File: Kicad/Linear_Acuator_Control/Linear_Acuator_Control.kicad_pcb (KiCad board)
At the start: 2 copper layers, 89.5 x 68 mm, 10 parts, among them K1 RT42xAxx, K3 RT42xAxx, Q1 IRLZ44N, Q2 IRLZ44N, U1 ESP32-S3-WROOM

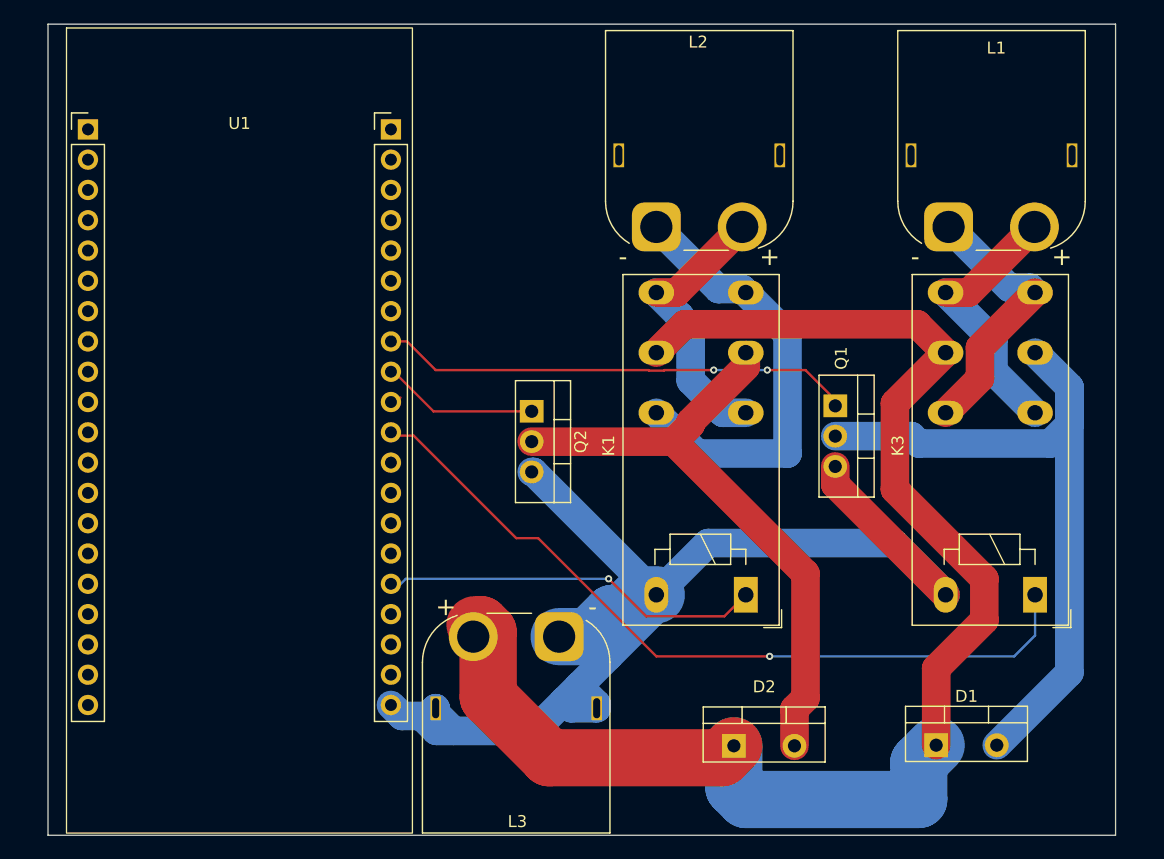
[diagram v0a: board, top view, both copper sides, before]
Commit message: Rerouting dodgy traces, fixing ESP32 footprint
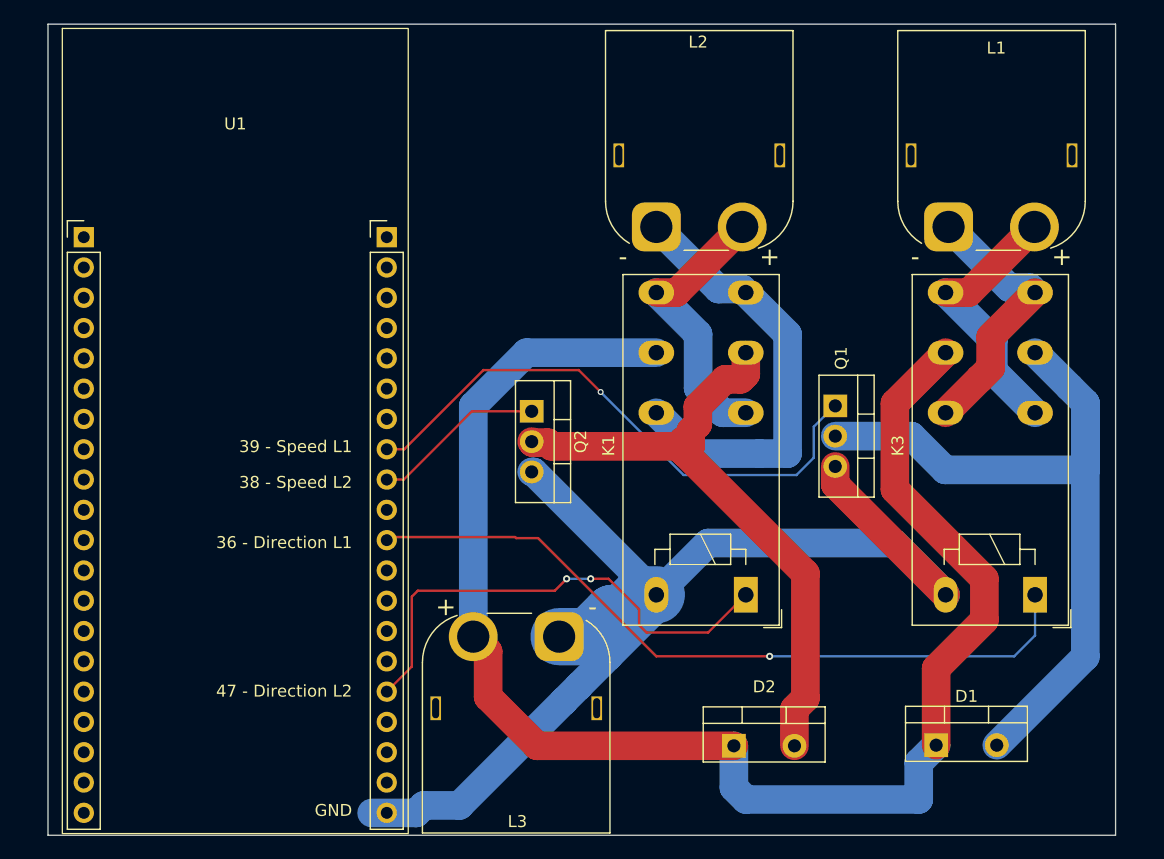
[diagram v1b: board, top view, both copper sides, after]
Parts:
- moved U1 0.56 mm to (79.2, 45.4)
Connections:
- net +3V3 renamed Net-(U1-3V3-Pad1)
- L3 pad : GND -> (no net)
- U1 pad 44: GND -> (no net)
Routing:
- net Dir L2: track 31.3 -> 41.4 mm, vias 1 -> 2
- net +24V: track 120.2 -> 129.3 mm
- net Speed L1: track 39.1 -> 48.0 mm, vias 2 -> 1
- net GND: track 107.5 -> 101.6 mm
- net Net-(D1-A): track 60.3 -> 65.6 mm
- net Dir L1: track 66.4 -> 62.7 mm
- net Net-(D2-A): track 52.1 -> 54.4 mm
- net Speed L2: track 13.4 -> 14.5 mm
- net unconnected-(U1-GPIO40/MTDO-Pad37): track 0.56 -> 0.00 mm
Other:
- board text added: "36 - Direction L1"
- board text added: "38 - Speed L2"
- board text added: "39 - Speed L1"
- board text added: "47 - Direction L2"
- board text added: "GND"

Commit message: Changed Mosfets to better suit 3.3v logic levels
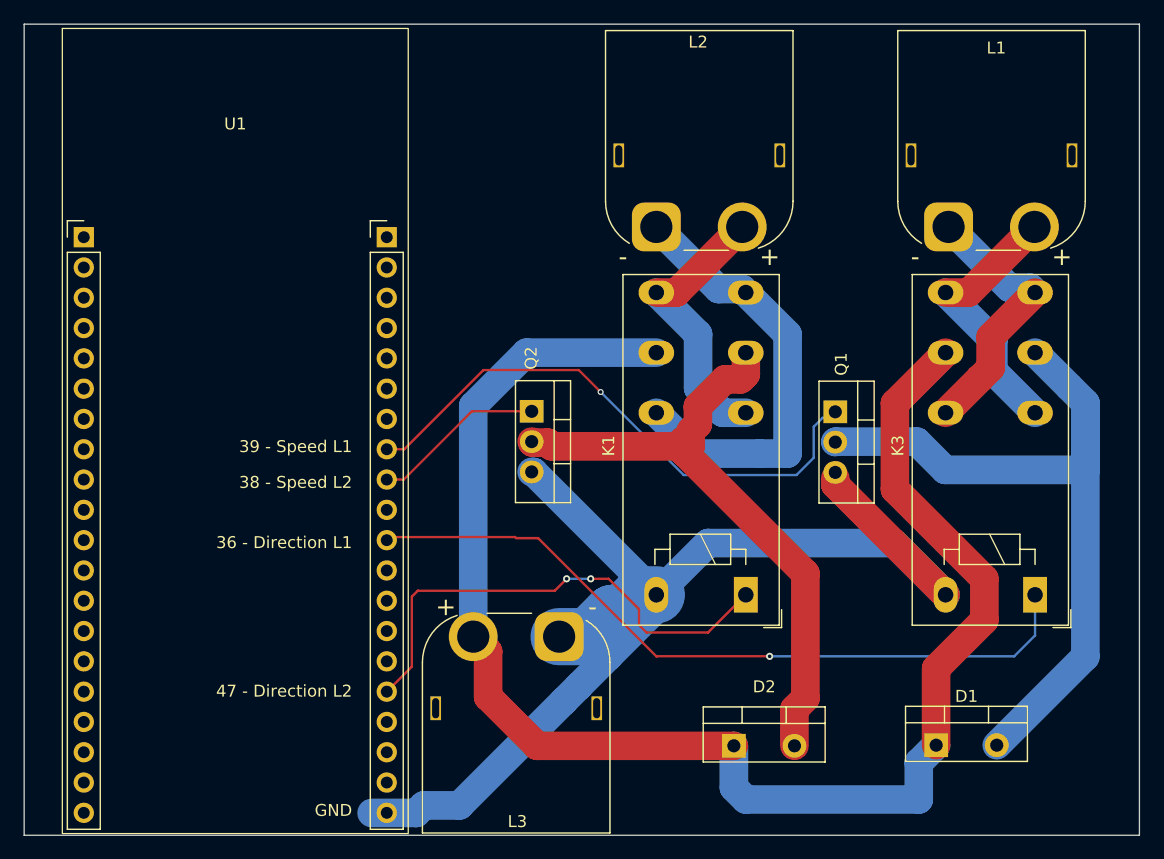
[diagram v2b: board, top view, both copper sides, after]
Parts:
- Q1, Q2: value IRLZ44N -> IRLB3813
- moved Q1 0.50 mm to (129.5, 69.5)
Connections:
- U1 pad 36: Dir L1 -> unconnected-(U1-GPIO39/MTCK-Pad36)
- U1 pad 39: Speed L1 -> unconnected-(U1-GPIO42/MTMS-Pad39)
- U1 pad 47: Dir L2 -> (no net)
- U1 pad GND: GND -> unconnected-(U1-PadGND)
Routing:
- net GND: track 101.6 -> 100.6 mm
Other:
- board size 89.5 x 68 mm -> 93.5 x 68 mm
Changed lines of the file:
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@@
 	(net 37 "unconnected-(U1-GPIO12{slash}ADC2_CH1-Pad18)")
 	(net 38 "Net-(U1-3V3-Pad1)")
+	(net 39 "unconnected-(U1-GPIO42{slash}MTMS-Pad39)")
+	(net 40 "unconnected-(U1-PadGND)")
+	(net 41 "unconnected-(U1-GPIO39{slash}MTCK-Pad36)")
 	(footprint "Relay_THT:Relay_DPDT_Schrack-RT2-FormC_RM5mm"
 		(layer "F.Cu")
@@
 		)
 		(property "Value" "RT42xAxx"
-			(at 12.192 4.25 90)
+			(at 0.84 4.5 90)
 			(layer "F.Fab")
 			(effects
@@
 	(footprint "Package_TO_SOT_THT:TO-220-3_Vertical"
 		(layer "F.Cu")
-		(at 129.5 69 -90)
+		(at 129.5 69.5 -90)
 		(descr "TO-220-3, Vertical, RM 2.54mm, see https://www.vishay.com/docs/66542/to-220-1.pdf, generated with kicad-footprint-generator TO_SOT_THT_generate.py")
 		(tags "TO-220-3 Vertical RM 2.54mm")
@@
 			)
 		)
-		(property "Value" "IRLZ44N"
+		(property "Value" "IRLB3813"
 			(at 2.54 2.2 90)
 			(layer "F.Fab")
@@
 		(tags "TO-220-3 Vertical RM 2.54mm")
 		(property "Reference" "Q2"
-			(at 2.54 -4.1 90)
+			(at -4.46 0.05 90)
 			(layer "F.SilkS")
 			(effects
@@
 			)
 		)
-		(property "Value" "IRLZ44N"
+		(property "Value" "IRLB3813"
 			(at 2.54 2.2 90)
 			(layer "F.Fab")
@@
 		)
 		(fp_text user "${REFERENCE}"
-			(at 0 2.98 0)
-			(unlocked yes)
+			(at 12.7 33.61 90)
 			(layer "F.Fab")
 			(effects
@@
 		)
 		(fp_text user "${REFERENCE}"
-			(at 12.7 33.61 90)
+			(at 0 2.98 0)
+			(unlocked yes)
 			(layer "F.Fab")
 			(effects
@@
 			(layers "*.Cu" "*.Mask")
 			(remove_unused_layers no)
-			(net 7 "Dir L1")
+			(net 41 "unconnected-(U1-GPIO39{slash}MTCK-Pad36)")
 			(pinfunction "GPIO39/MTCK")
 			(pintype "bidirectional")
@@
 			(layers "*.Cu" "*.Mask")
 			(remove_unused_layers no)
-			(net 11 "Speed L1")
+			(net 39 "unconnected-(U1-GPIO42{slash}MTMS-Pad39)")
 			(pinfunction "GPIO42/MTMS")
 			(pintype "bidirectional")
@@
 			(layers "*.Cu" "*.Mask")
 			(remove_unused_layers no)
-			(net 9 "Dir L2")
 		)
 		(pad "48" thru_hole circle
@@
 			(layers "*.Cu" "*.Mask")
 			(remove_unused_layers no)
-			(net 6 "GND")
+			(net 40 "unconnected-(U1-PadGND)")
 			(pinfunction "GND")
 			(pintype "power_in")
@@
 	)
 	(gr_line
-		(start 63.5 105)
-		(end 63.5 37)
+		(start 61.5 105)
+		(end 61.5 37)
 		(stroke
 			(width 0.05)
@@
 	)
 	(gr_line
-		(start 153 105)
-		(end 63.5 105)
+		(start 155 105)
+		(end 61.5 105)
 		(stroke
 			(width 0.05)
@@
 	)
 	(gr_line
-		(start 63.5 37)
-		(end 153 37)
+		(start 61.5 37)
+		(end 155 37)
 		(stroke
 			(width 0.05)
@@
 	)
 	(gr_line
-		(start 153 37)
-		(end 153 105)
+		(start 155 37)
+		(end 155 105)
 		(stroke
 			(width 0.05)
@@
 	)
 	(segment
-		(start 137.96 91.007266)
-		(end 137.96 97.45)
-		(width 2.4)
-		(layer "F.Cu")
-		(net 1)
-	)
-	(segment
 		(start 100.4 89.6)
 		(end 99.15 88.35)
@@
 	)
 	(segment
-		(start 142 86.967266)
-		(end 137.96 91.007266)
+		(start 142 83.5)
+		(end 142 86.967266)
 		(width 2.4)
 		(layer "F.Cu")
@@
 	)
 	(segment
-		(start 134.5 76)
-		(end 142 83.5)
+		(start 134.5 68.79)
+		(end 134.5 76)
 		(width 2.4)
 		(layer "F.Cu")
@@
 	)
 	(segment
-		(start 142 83.5)
-		(end 142 86.967266)
+		(start 142 86.967266)
+		(end 137.96 91.007266)
+		(width 2.4)
+		(layer "F.Cu")
+		(net 1)
+	)
+	(segment
+		(start 134.5 76)
+		(end 142 83.5)
 		(width 2.4)
 		(layer "F.Cu")
@@
 	)
 	(segment
-		(start 134.5 68.79)
-		(end 134.5 76)
+		(start 137.96 91.007266)
+		(end 137.96 97.45)
 		(width 2.4)
 		(layer "F.Cu")
@@
 	)
 	(segment
-		(start 135.885 71.54)
-		(end 138.714117 74.369117)
+		(start 138.714117 74.369117)
+		(end 150.407917 74.369117)
 		(width 2.4)
 		(layer "B.Cu")
@@
 	)
 	(segment
-		(start 150.407917 74.369117)
-		(end 150.465945 74.427145)
+		(start 150.465945 90.024055)
+		(end 150.465945 68.755945)
 		(width 2.4)
 		(layer "B.Cu")
@@
 	)
 	(segment
-		(start 129.5 71.54)
-		(end 135.885 71.54)
+		(start 136.345 72)
+		(end 138.714117 74.369117)
 		(width 2.4)
 		(layer "B.Cu")
@@
 	)
 	(segment
-		(start 138.714117 74.369117)
-		(end 150.407917 74.369117)
+		(start 150.465945 68.755945)
+		(end 149.1288 67.4188)
 		(width 2.4)
 		(layer "B.Cu")
@@
 	)
 	(segment
-		(start 150.465945 90.024055)
-		(end 150.465945 68.755945)
+		(start 129.5 72.04)
+		(end 129.54 72)
 		(width 2.4)
 		(layer "B.Cu")
@@
 	)
 	(segment
-		(start 150.465945 68.755945)
-		(end 149.1288 67.4188)
+		(start 143.04 97.45)
+		(end 150.465945 90.024055)
 		(width 2.4)
 		(layer "B.Cu")
@@
 	)
 	(segment
-		(start 143.04 97.45)
-		(end 150.465945 90.024055)
+		(start 149.1288 67.4188)
+		(end 146.25 64.54)
 		(width 2.4)
 		(layer "B.Cu")
@@
 	)
 	(segment
-		(start 149.1288 67.4188)
-		(end 146.25 64.54)
+		(start 129.54 72)
+		(end 136.345 72)
+		(width 2.4)
+		(layer "B.Cu")
+		(net 2)
+	)
+	(segment
+		(start 150.407917 74.369117)
+		(end 150.465945 74.427145)
 		(width 2.4)
 		(layer "B.Cu")
@@
 	)
 	(segment
-		(start 129.5 74.08)
+		(start 129.5 75.08)
 		(end 129.5 75.59)
 		(width 2.4)
@@
 	)
 	(segment
-		(start 127.699 70.7535)
-		(end 129.4525 69)
+		(start 116.791 74.801)
+		(end 126.245999 74.801)
 		(width 0.2)
 		(layer "B.Cu")
@@
 	)
 	(segment
-		(start 109.83 67.84)
-		(end 116.791 74.801)
+		(start 127.699 73.347999)
+		(end 127.699 70.7535)
 		(width 0.2)
 		(layer "B.Cu")
@@
 	)
 	(segment
-		(start 116.791 74.801)
-		(end 126.245999 74.801)
+		(start 126.245999 74.801)
+		(end 127.699 73.347999)
 		(width 0.2)
 		(layer "B.Cu")
@@
 	)
 	(segment
-		(start 126.245999 74.801)
-		(end 127.699 73.347999)
+		(start 127.699 70.7535)
+		(end 128.4525 70)
 		(width 0.2)
 		(layer "B.Cu")
@@
 	)
 	(segment
-		(start 129.4525 69)
-		(end 129.5 69)
+		(start 109.83 67.84)
+		(end 116.791 74.801)
 		(width 0.2)
 		(layer "B.Cu")
@@
 	)
 	(segment
-		(start 127.699 73.347999)
-		(end 127.699 70.7535)
+		(start 128.4525 70)
+		(end 129.5 70)
 		(width 0.2)
 		(layer "B.Cu")
